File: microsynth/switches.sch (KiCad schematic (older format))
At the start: 37 parts, among them SW12 SOURCE, SW13 THUMBWEEL, SW14 SW_SPDT, SW15 SW_SPDT, SW16 SW_SPDT, SW17 SW_SPDT, SW2 RANGE, SW21 SW_Rotary2x6, SW3 SW_DPTT_SELECTOR, SW4 SW_DPTT_SELECTOR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

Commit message: Consolidate switches
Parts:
- SW12: value SOURCE -> SW_DP3T; footprint Buttons_Switches_ThroughHole:G-1128S-1110 -> microsynth:11-SS-23-832C; Value (none) -> THUMBWHEEL SOURCE
- SW13: value THUMBWEEL -> SW_DP3T; footprint Buttons_Switches_ThroughHole:G-1128S-1110 -> microsynth:11-SS-23-832C; Value (none) -> THUMBWHEEL DEST
- SW14, SW15, SW16, SW17, SW5: footprint Buttons_Switches_ThroughHole:GF-624-6014 -> microsynth:11-SS-22-701C
- SW2: value RANGE -> SW_Rotary2x6; Label Range -> VCO RANGE
- SW21: footprint Button_Switch_THT:SR2612F-0304-18R0B-D8-N -> microsynth:SR2612F-0304-18R0B-D8-N; Label (none) -> VCO2_SHAPE
- SW3, SW4, SW6: value SW_DPTT_SELECTOR -> SW_DP3T; footprint Buttons_Switches_ThroughHole:G-1128S-1110 -> microsynth:11-SS-23-832C
- SW3: value SW_DPTT_SELECTOR -> SW_DP3T; footprint Buttons_Switches_ThroughHole:G-1128S-1110 -> microsynth:11-SS-23-832C; Value (none) -> VCO1 SHAPE
- SW4: value SW_DPTT_SELECTOR -> SW_DP3T; footprint Buttons_Switches_ThroughHole:G-1128S-1110 -> microsynth:11-SS-23-832C; Label (none) -> SUBOCTAVES
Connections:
- wire segments 203 -> 199
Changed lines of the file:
@@
 AR Path="/5E475532/5E4ABA98" Ref="SW6"  Part="2"
 F 0 "SW6" H 6294 3079 50  0000 L CNN
-F 1 "SW_DPTT_SELECTOR" H 6294 2988 50  0000 L CNN
-F 2 "Buttons_Switches_ThroughHole:G-1128S-1110" H 6100 2950 50  0001 C CNN
+F 1 "SW_DP3T" H 6294 2988 50  0000 L CNN
+F 2 "microsynth:11-SS-23-832C" H 6100 2950 50  0001 C CNN
 F 3 "" H 6100 2950 50  0001 C CNN
 	2    6100 2950
@@
 AR Path="/5E475532/5E4BC6EF" Ref="SW3"  Part="1"
 F 0 "SW3" H 7594 1338 50  0000 L CNN
-F 1 "SW_DPTT_SELECTOR" H 7594 1247 50  0000 L CNN
-F 2 "Buttons_Switches_ThroughHole:G-1128S-1110" H 7400 1350 50  0001 C CNN
+F 1 "SW_DP3T" H 7594 1247 50  0000 L CNN
+F 2 "microsynth:11-SS-23-832C" H 7400 1350 50  0001 C CNN
 F 3 "" H 7400 1350 50  0001 C CNN
 	1    7400 1350
@@
 AR Path="/5E475532/5E4BCFE7" Ref="SW3"  Part="2"
 F 0 "SW3" H 7594 1379 50  0000 L CNN
-F 1 "SW_DPTT_SELECTOR" H 7594 1288 50  0000 L CNN
-F 2 "Buttons_Switches_ThroughHole:G-1128S-1110" H 7400 1250 50  0001 C CNN
+F 1 "SW_DP3T" H 7594 1288 50  0000 L CNN
+F 2 "microsynth:11-SS-23-832C" H 7400 1250 50  0001 C CNN
 F 3 "" H 7400 1250 50  0001 C CNN
+F 4 "VCO1 SHAPE" H 8050 1400 50  0000 C CNN "Value"
 	2    7400 1250
 	1    0    0    -1
@@
 AR Path="/5E475532/5E4C21F7" Ref="SW4"  Part="1"
 F 0 "SW4" H 9344 1338 50  0000 L CNN
-F 1 "SW_DPTT_SELECTOR" H 9344 1247 50  0000 L CNN
-F 2 "Buttons_Switches_ThroughHole:G-1128S-1110" H 9150 1350 50  0001 C CNN
+F 1 "SW_DP3T" H 9344 1247 50  0000 L CNN
+F 2 "microsynth:11-SS-23-832C" H 9150 1350 50  0001 C CNN
 F 3 "" H 9150 1350 50  0001 C CNN
 	1    9150 1350
-	1    0    0    -1
-$EndComp
-$Comp
-L microsynth-rescue:SW_DPTT_SELECTOR-Switch SW4
-U 2 1 5E4C2687
-P 9150 1250
-AR Path="/5E4C2687" Ref="SW4"  Part="2"
-AR Path="/5E475532/5E4C2687" Ref="SW4"  Part="2"
-F 0 "SW4" H 9344 1379 50  0000 L CNN
-F 1 "SW_DPTT_SELECTOR" H 9344 1288 50  0000 L CNN
-F 2 "Buttons_Switches_ThroughHole:G-1128S-1110" H 9150 1250 50  0001 C CNN
-F 3 "" H 9150 1250 50  0001 C CNN
-	2    9150 1250
 	1    0    0    -1
 $EndComp
@@
 NoConn ~ 9100 1550
 Wire Wire Line
-	9100 1050 9100 1300
-Wire Wire Line
-	9100 1300 9200 1300
-Wire Wire Line
-	9200 1300 9200 1550
-Wire Wire Line
-	9300 1550 9300 1250
-Wire Wire Line
-	9300 1250 9200 1250
-Wire Wire Line
-	9200 1250 9200 1050
-Wire Wire Line
 	7450 1550 7450 1750
 Wire Wire Line
@@
 Connection ~ 8550 1750
 Wire Wire Line
-	9300 1750 9300 1550
-Wire Wire Line
 	8550 1750 9300 1750
-Connection ~ 9300 1550
 $Comp
 L Device:R R80
@@
 Wire Wire Line
 	9200 1900 9200 1550
-Connection ~ 9200 1550
 Wire Wire Line
 	9300 1050 9300 950
@@
 U 1 1 5E4E1AE1
 P 9650 3100
-F 0 "U22" H 9650 3581 50  0000 C CNN
-F 1 "4013" H 9650 3490 50  0000 C CNN
+F 0 "U22" H 9700 3100 50  0000 C CNN
+F 1 "4013" H 9800 3350 50  0000 C CNN
 F 2 "Package_DIP:DIP-14_W7.62mm_LongPads" H 9650 3100 50  0001 C CNN
 F 3 "http://www.onsemi.com/pub/Collateral/MC14013B-D.PDF" H 9650 3100 50  0001 C CNN
@@
 F 0 "SW5" V 10604 1112 50  0000 R CNN
 F 1 "SW_SPDT" V 10695 1112 50  0000 R CNN
-F 2 "Buttons_Switches_ThroughHole:GF-624-6014" H 10650 1300 50  0001 C CNN
+F 2 "microsynth:11-SS-22-701C" H 10650 1300 50  0001 C CNN
 F 3 "~" H 10650 1300 50  0001 C CNN
 	1    10650 1300
@@
 U 2 1 5E4E234D
 P 9650 4350
-F 0 "U22" H 9650 4831 50  0000 C CNN
-F 1 "4013" H 9650 4740 50  0000 C CNN
+F 0 "U22" H 9700 4350 50  0000 C CNN
+F 1 "4013" H 9500 4600 50  0000 C CNN
 F 2 "Package_DIP:DIP-14_W7.62mm_LongPads" H 9650 4350 50  0001 C CNN
 F 3 "http://www.onsemi.com/pub/Collateral/MC14013B-D.PDF" H 9650 4350 50  0001 C CNN
@@
 P 1700 6350
 F 0 "SW2" H 1750 7221 50  0000 C CNN
-F 1 "RANGE" H 1750 7130 50  0000 C CNN
+F 1 "SW_Rotary2x6" H 1750 7130 50  0000 C CNN
 F 2 "MyKi_TH_Panel_Controls:SW_Rotary4+12" H 1600 6950 50  0001 C CNN
 F 3 "https://www.tme.eu/Document/ecc8d6706892f543e4658b0fb9f5b772/sr261112.pdf" H 1600 6950 50  0001 C CNN
-F 4 "Range" H 1750 7039 50  0000 C CNN "Label"
+F 4 "VCO RANGE" H 1750 7039 50  0000 C CNN "Label"
 F 5 "SR26NS1-2-6-M10-38R6" H 1700 6350 50  0001 C CNN "Product#"
 	1    1700 6350
@@
 AR Path="/5E475532/5E4A877E" Ref="SW6"  Part="1"
 F 0 "SW6" H 2894 2738 50  0000 L CNN
-F 1 "SW_DPTT_SELECTOR" H 2894 2647 50  0000 L CNN
-F 2 "Buttons_Switches_ThroughHole:G-1128S-1110" H 2700 2750 50  0001 C CNN
+F 1 "SW_DP3T" H 2894 2647 50  0000 L CNN
+F 2 "microsynth:11-SS-23-832C" H 2700 2750 50  0001 C CNN
 F 3 "" H 2700 2750 50  0001 C CNN
 	1    2700 2750
@@
 F 0 "SW17" H 3600 2635 50  0000 C CNN
 F 1 "SW_SPDT" H 3600 2544 50  0000 C CNN
-F 2 "Buttons_Switches_ThroughHole:GF-624-6014" H 3600 2350 50  0001 C CNN
+F 2 "microsynth:11-SS-22-701C" H 3600 2350 50  0001 C CNN
 F 3 "~" H 3600 2350 50  0001 C CNN
 	1    3600 2350
@@
 F 0 "SW16" H 3600 2135 50  0000 C CNN
 F 1 "SW_SPDT" H 3600 2044 50  0000 C CNN
-F 2 "Buttons_Switches_ThroughHole:GF-624-6014" H 3600 1850 50  0001 C CNN
+F 2 "microsynth:11-SS-22-701C" H 3600 1850 50  0001 C CNN
 F 3 "~" H 3600 1850 50  0001 C CNN
 	1    3600 1850
@@
 F 0 "SW15" H 3600 1635 50  0000 C CNN
 F 1 "SW_SPDT" H 3600 1544 50  0000 C CNN
-F 2 "Buttons_Switches_ThroughHole:GF-624-6014" H 3600 1350 50  0001 C CNN
+F 2 "microsynth:11-SS-22-701C" H 3600 1350 50  0001 C CNN
 F 3 "~" H 3600 1350 50  0001 C CNN
 	1    3600 1350
@@
 F 0 "SW14" H 3600 1135 50  0000 C CNN
 F 1 "SW_SPDT" H 3600 1044 50  0000 C CNN
-F 2 "Buttons_Switches_ThroughHole:GF-624-6014" H 3600 850 50  0001 C CNN
+F 2 "microsynth:11-SS-22-701C" H 3600 850 50  0001 C CNN
 F 3 "~" H 3600 850 50  0001 C CNN
 	1    3600 850
@@
 AR Path="/5E475532/5EC4EDF0" Ref="SW12"  Part="1"
 F 0 "SW12" H 5594 4488 50  0000 L CNN
-F 1 "SOURCE" H 5594 4397 50  0000 L CNN
-F 2 "Buttons_Switches_ThroughHole:G-1128S-1110" H 5400 4500 50  0001 C CNN
+F 1 "SW_DP3T" H 5594 4397 50  0000 L CNN
+F 2 "microsynth:11-SS-23-832C" H 5400 4500 50  0001 C CNN
 F 3 "" H 5400 4500 50  0001 C CNN
+F 4 "THUMBWHEEL SOURCE" H 5600 4900 50  0000 C CNN "Value"
 	1    5400 4500
 	1    0    0    -1
@@
 AR Path="/5E475532/5EC508E1" Ref="SW12"  Part="2"
 F 0 "SW12" H 5594 4629 50  0000 L CNN
-F 1 "SOURCE" H 5594 4538 50  0000 L CNN
-F 2 "Buttons_Switches_ThroughHole:G-1128S-1110" H 5400 4500 50  0001 C CNN
+F 1 "SW_DP3T" H 5594 4538 50  0000 L CNN
+F 2 "microsynth:11-SS-23-832C" H 5400 4500 50  0001 C CNN
 F 3 "" H 5400 4500 50  0001 C CNN
+F 4 "THUMBWHEEL SOURCE" H 5600 4900 50  0000 C CNN "Value"
 	2    5400 4500
 	1    0    0    -1
@@
 AR Path="/5E475532/5EC8F4DB" Ref="SW13"  Part="1"
 F 0 "SW13" H 7394 4438 50  0000 L CNN
-F 1 "THUMBWEEL" H 7394 4347 50  0000 L CNN
-F 2 "Buttons_Switches_ThroughHole:G-1128S-1110" H 7200 4450 50  0001 C CNN
+F 1 "SW_DP3T" H 7394 4347 50  0000 L CNN
+F 2 "microsynth:11-SS-23-832C" H 7200 4450 50  0001 C CNN
 F 3 "" H 7200 4450 50  0001 C CNN
+F 4 "THUMBWHEEL DEST" H 7200 4850 50  0000 C CNN "Value"
 	1    7200 4450
 	1    0    0    -1
@@
 AR Path="/5E475532/5EC90227" Ref="SW13"  Part="2"
 F 0 "SW13" H 7394 4579 50  0000 L CNN
-F 1 "THUMBWEEL" H 7394 4488 50  0000 L CNN
-F 2 "Buttons_Switches_ThroughHole:G-1128S-1110" H 7200 4450 50  0001 C CNN
+F 1 "SW_DP3T" H 7394 4488 50  0000 L CNN
+F 2 "microsynth:11-SS-23-832C" H 7200 4450 50  0001 C CNN
 F 3 "" H 7200 4450 50  0001 C CNN
+F 4 "THUMBWHEEL DEST" H 7200 4850 50  0000 C CNN "Value"
 	2    7200 4450
 	1    0    0    -1
@@
 F 0 "SW21" H 1850 2831 50  0000 C CNN
 F 1 "SW_Rotary2x6" H 1850 2740 50  0000 C CNN
-F 2 "Button_Switch_THT:SR2612F-0304-18R0B-D8-N" H 1700 2650 50  0001 C CNN
+F 2 "microsynth:SR2612F-0304-18R0B-D8-N" H 1700 2650 50  0001 C CNN
 F 3 "https://www.taydaelectronics.com/datasheets/A-1891.pdf" H 1700 2650 50  0001 C CNN
+F 4 "VCO2_SHAPE" H 1400 2850 50  0000 C CNN "Label"
 	1    1800 2050
 	-1   0    0    -1
@@
 NoConn ~ 1300 2550
 NoConn ~ 1300 2650
+Wire Wire Line
+	9300 1750 9300 1550
+$Comp
+L microsynth-rescue:SW_DPTT_SELECTOR-Switch SW4
+U 2 1 5E4C2687
+P 9150 1250
+AR Path="/5E4C2687" Ref="SW4"  Part="2"
+AR Path="/5E475532/5E4C2687" Ref="SW4"  Part="2"
+F 0 "SW4" H 9344 1379 50  0000 L CNN
+F 1 "SW_DP3T" H 9344 1288 50  0000 L CNN
+F 2 "microsynth:11-SS-23-832C" H 9150 1250 50  0001 C CNN
+F 3 "" H 9150 1250 50  0001 C CNN
+F 4 "SUBOCTAVES" H 9250 1600 50  0000 C CNN "Label"
+	2    9150 1250
+	1    0    0    -1
+$EndComp
+Wire Wire Line
+	9300 1550 9200 1050
+Connection ~ 9300 1550
+Wire Wire Line
+	9200 1550 9100 1050
+Connection ~ 9200 1550
 $EndSCHEMATC

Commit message: Consolidate all(?) switches
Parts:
- RV20, RV28: footprint 4ms_Potentiometer:Pot_16mm_NoDet_RV16AF-4A -> microsynth:Pot_16mm_NoDet_RV16AF-4A
- SW12, SW13, SW3, SW4, SW6: symbol microsynth-rescue:SW_DPTT_SELECTOR-Switch -> pe_microsynth:SW_DPTT_SELECTOR-Switch
- SW2: footprint MyKi_TH_Panel_Controls:SW_Rotary4+12 -> microsynth:SW_Rotary4+12
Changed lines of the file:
@@
 $EndDescr
 $Comp
-L microsynth-rescue:SW_DPTT_SELECTOR-Switch SW6
+L pe_microsynth:SW_DPTT_SELECTOR-Switch SW6
 U 2 1 5E4ABA98
 P 6100 2950
@@
 $EndComp
 $Comp
-L microsynth-rescue:SW_DPTT_SELECTOR-Switch SW3
+L pe_microsynth:SW_DPTT_SELECTOR-Switch SW3
 U 1 1 5E4BC6EF
 P 7400 1350
@@
 $EndComp
 $Comp
-L microsynth-rescue:SW_DPTT_SELECTOR-Switch SW3
+L pe_microsynth:SW_DPTT_SELECTOR-Switch SW3
 U 2 1 5E4BCFE7
 P 7400 1250
@@
 NoConn ~ 7250 1550
 $Comp
-L microsynth-rescue:SW_DPTT_SELECTOR-Switch SW4
+L pe_microsynth:SW_DPTT_SELECTOR-Switch SW4
 U 1 1 5E4C21F7
 P 9150 1350
@@
 F 0 "SW2" H 1750 7221 50  0000 C CNN
 F 1 "SW_Rotary2x6" H 1750 7130 50  0000 C CNN
-F 2 "MyKi_TH_Panel_Controls:SW_Rotary4+12" H 1600 6950 50  0001 C CNN
+F 2 "microsynth:SW_Rotary4+12" H 1600 6950 50  0001 C CNN
 F 3 "https://www.tme.eu/Document/ecc8d6706892f543e4658b0fb9f5b772/sr261112.pdf" H 1600 6950 50  0001 C CNN
 F 4 "VCO RANGE" H 1750 7039 50  0000 C CNN "Label"
@@
 	2200 2050 2400 2050
 $Comp
-L microsynth-rescue:SW_DPTT_SELECTOR-Switch SW6
+L pe_microsynth:SW_DPTT_SELECTOR-Switch SW6
 U 1 1 5E4A877E
 P 2700 2750
@@
 F 0 "RV20" H 2480 1746 50  0000 R CNN
 F 1 "10kLOG" H 2480 1655 50  0000 R CNN
-F 2 "4ms_Potentiometer:Pot_16mm_NoDet_RV16AF-4A" H 2550 1700 50  0001 C CNN
+F 2 "microsynth:Pot_16mm_NoDet_RV16AF-4A" H 2550 1700 50  0001 C CNN
 F 3 "~" H 2550 1700 50  0001 C CNN
 F 4 "VCO2 Level" H 2450 1800 50  0000 R BNN "Label"
@@
 F 0 "RV28" H 3980 4646 50  0000 R CNN
 F 1 "1kLIN" H 3980 4555 50  0000 R CNN
-F 2 "4ms_Potentiometer:Pot_16mm_NoDet_RV16AF-4A" H 4050 4600 50  0001 C CNN
+F 2 "microsynth:Pot_16mm_NoDet_RV16AF-4A" H 4050 4600 50  0001 C CNN
 F 3 "~" H 4050 4600 50  0001 C CNN
 F 4 "Sweep" H 3950 4450 50  0000 R BNN "Label"
@@
 	6400 5000 6400 4900
 $Comp
-L microsynth-rescue:SW_DPTT_SELECTOR-Switch SW12
+L pe_microsynth:SW_DPTT_SELECTOR-Switch SW12
 U 1 1 5EC4EDF0
 P 5400 4500
@@
 $EndComp
 $Comp
-L microsynth-rescue:SW_DPTT_SELECTOR-Switch SW12
+L pe_microsynth:SW_DPTT_SELECTOR-Switch SW12
 U 2 1 5EC508E1
 P 5400 4500
@@
 	5550 3900 4950 3900
 $Comp
-L microsynth-rescue:SW_DPTT_SELECTOR-Switch SW13
+L pe_microsynth:SW_DPTT_SELECTOR-Switch SW13
 U 1 1 5EC8F4DB
 P 7200 4450
@@
 $EndComp
 $Comp
-L microsynth-rescue:SW_DPTT_SELECTOR-Switch SW13
+L pe_microsynth:SW_DPTT_SELECTOR-Switch SW13
 U 2 1 5EC90227
 P 7200 4450
@@
 	9300 1750 9300 1550
 $Comp
-L microsynth-rescue:SW_DPTT_SELECTOR-Switch SW4
+L pe_microsynth:SW_DPTT_SELECTOR-Switch SW4
 U 2 1 5E4C2687
 P 9150 1250

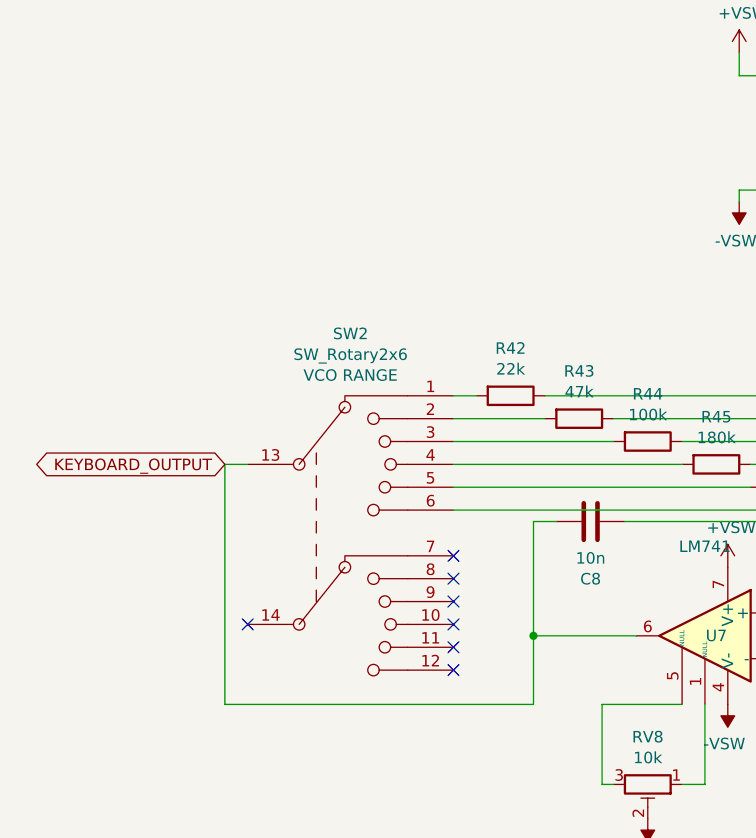
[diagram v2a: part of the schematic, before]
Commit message: Update tayda rotary switch footprints and layout
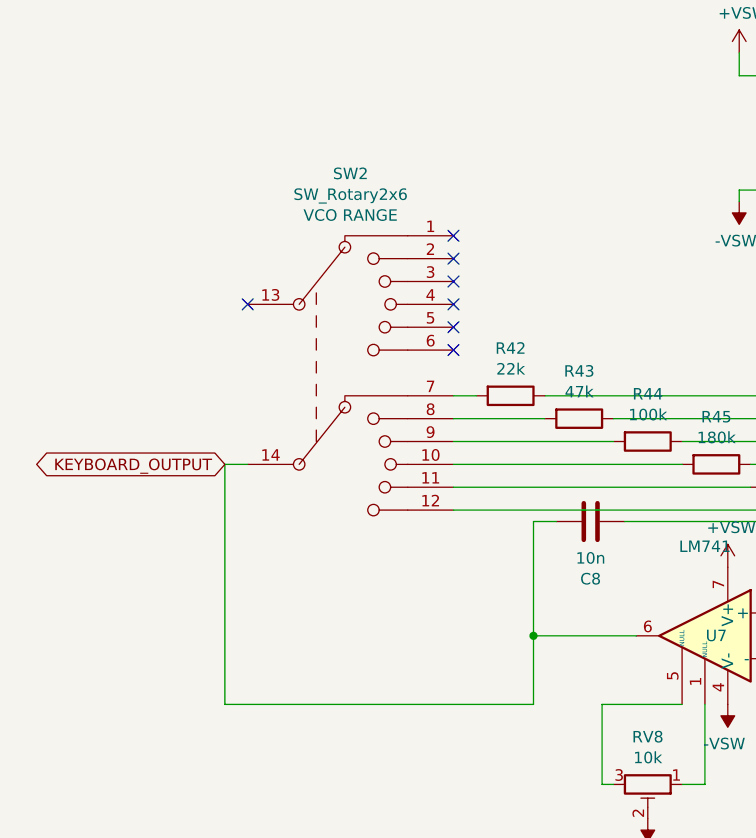
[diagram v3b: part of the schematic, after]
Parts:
- SW2: footprint microsynth:SW_Rotary4+12 -> microsynth:SR2511F-0206-(L)K0A-C9-S-3
- SW21: footprint microsynth:SR2612F-0304-18R0B-D8-N -> microsynth:SR2511F-0204-(L)K0A-C9-S-3
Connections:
- net KEYBOARD_IC7_PIN_6: now also SW2.14; no longer SW2.13
- net at SW2.1: no longer R42.2
- net at SW2.10: now also R45.2
- net at SW2.11: now also R46.1
- net at SW2.12: now also R46-1.1
- net at SW2.2: no longer R43.2
- net at SW2.3: no longer R44.2
- net at SW2.4: no longer R45.2
- net at SW2.5: no longer R46.1
- net at SW2.6: no longer R46-1.1
- net at SW2.7: now also R42.2
- net at SW2.8: now also R43.2
- net at SW2.9: now also R44.2
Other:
- moved on the sheet: SW2
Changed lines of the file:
@@
 Wire Wire Line
 	9350 3100 8800 3100
-NoConn ~ 2200 6850
-NoConn ~ 2200 6750
-NoConn ~ 2200 6650
-NoConn ~ 2200 6550
-NoConn ~ 2200 6450
-NoConn ~ 1300 6750
+NoConn ~ 2200 5450
+NoConn ~ 2200 5350
+NoConn ~ 2200 5250
+NoConn ~ 2200 5150
+NoConn ~ 2200 5050
+NoConn ~ 1300 5350
 $Comp
 L Switch:SW_Rotary2x6 SW2
 U 1 1 5E4793CB
-P 1700 6350
-F 0 "SW2" H 1750 7221 50  0000 C CNN
-F 1 "SW_Rotary2x6" H 1750 7130 50  0000 C CNN
-F 2 "microsynth:SW_Rotary4+12" H 1600 6950 50  0001 C CNN
-F 3 "https://www.tme.eu/Document/ecc8d6706892f543e4658b0fb9f5b772/sr261112.pdf" H 1600 6950 50  0001 C CNN
-F 4 "VCO RANGE" H 1750 7039 50  0000 C CNN "Label"
-F 5 "SR26NS1-2-6-M10-38R6" H 1700 6350 50  0001 C CNN "Product#"
-	1    1700 6350
+P 1700 5650
+F 0 "SW2" H 1750 6521 50  0000 C CNN
+F 1 "SW_Rotary2x6" H 1750 6430 50  0000 C CNN
+F 2 "microsynth:SR2511F-0206-(L)K0A-C9-S-3" H 1600 6250 50  0001 C CNN
+F 3 "https://www.tme.eu/Document/ecc8d6706892f543e4658b0fb9f5b772/sr261112.pdf" H 1600 6250 50  0001 C CNN
+F 4 "VCO RANGE" H 1750 6339 50  0000 C CNN "Label"
+F 5 "SR26NS1-2-6-M10-38R6" H 1700 5650 50  0001 C CNN "Product#"
+	1    1700 5650
 	1    0    0    -1
 $EndComp
@@
 NoConn ~ 2750 2950
 NoConn ~ 2850 2950
-NoConn ~ 2200 6950
+NoConn ~ 2200 5550
 Wire Wire Line
 	3200 5950 4500 5950
@@
 F 0 "SW21" H 1850 2831 50  0000 C CNN
 F 1 "SW_Rotary2x6" H 1850 2740 50  0000 C CNN
-F 2 "microsynth:SR2612F-0304-18R0B-D8-N" H 1700 2650 50  0001 C CNN
+F 2 "microsynth:SR2511F-0204-(L)K0A-C9-S-3" H 1700 2650 50  0001 C CNN
 F 3 "https://www.taydaelectronics.com/datasheets/A-1891.pdf" H 1700 2650 50  0001 C CNN
 F 4 "VCO2_SHAPE" H 1400 2850 50  0000 C CNN "Label"

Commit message: Add test points
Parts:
- added TP4: VCO2, TestPoint:TestPoint_Pad_D2.0mm, symbol Connector:TestPoint
- added TP5: VCO1, TestPoint:TestPoint_Pad_D2.0mm, symbol Connector:TestPoint
- SW21: symbol Switch:SW_Rotary3x4 -> pe_microsynth:SW_Rotary2x4
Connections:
- net LFO_TO_VR20_SLIDER: now also TP4.1
- net TO_VCF_IC20_3: now also TP5.1
- no-connect marks 28 -> 23
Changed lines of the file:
@@
 	7450 1550 7450 1750
 Wire Wire Line
-	7450 1750 8550 1750
+	7450 1750 7950 1750
 Wire Wire Line
 	6950 800  7350 800
@@
 Connection ~ 3250 1700
 Wire Wire Line
-	2700 1700 3250 1700
+	2700 1700 2800 1700
 Connection ~ 3250 1850
 Wire Wire Line
@@
 	3800 6250 2200 6250
 $Comp
-L Switch:SW_Rotary3x4 SW21
+L pe_microsynth:SW_Rotary2x4 SW21
 U 1 1 5E476048
-P 1800 2050
-F 0 "SW21" H 1850 2831 50  0000 C CNN
-F 1 "SW_Rotary2x6" H 1850 2740 50  0000 C CNN
-F 2 "microsynth:SR2511F-0204-(L)K0A-C9-S-3" H 1700 2650 50  0001 C CNN
-F 3 "https://www.taydaelectronics.com/datasheets/A-1891.pdf" H 1700 2650 50  0001 C CNN
-F 4 "VCO2_SHAPE" H 1400 2850 50  0000 C CNN "Label"
-	1    1800 2050
+P 1800 1700
+F 0 "SW21" H 1850 2481 50  0000 C CNN
+F 1 "SW_Rotary2x6" H 1850 2390 50  0000 C CNN
+F 2 "microsynth:SR2511F-0204-(L)K0A-C9-S-3" H 1700 2300 50  0001 C CNN
+F 3 "https://www.taydaelectronics.com/datasheets/A-1891.pdf" H 1700 2300 50  0001 C CNN
+F 4 "VCO2_SHAPE" H 1400 2500 50  0000 C CNN "Label"
+	1    1800 1700
 	-1   0    0    -1
 $EndComp
-NoConn ~ 2200 2550
-NoConn ~ 1300 2350
-NoConn ~ 1300 2450
-NoConn ~ 1300 2550
-NoConn ~ 1300 2650
 Wire Wire Line
 	9300 1750 9300 1550
@@
 	9200 1550 9100 1050
 Connection ~ 9200 1550
+$Comp
+L Connector:TestPoint TP5
+U 1 1 5EDEA929
+P 7950 1750
+F 0 "TP5" H 8050 1900 50  0000 L CNN
+F 1 "VCO1" H 8050 1800 50  0000 L CNN
+F 2 "TestPoint:TestPoint_Pad_D2.0mm" H 8150 1750 50  0001 C CNN
+F 3 "~" H 8150 1750 50  0001 C CNN
+	1    7950 1750
+	1    0    0    -1
+$EndComp
+Connection ~ 7950 1750
+Wire Wire Line
+	7950 1750 8550 1750
+$Comp
+L Connector:TestPoint TP4
+U 1 1 5EDEAFEB
+P 2800 1700
+F 0 "TP4" H 2900 1850 50  0000 L CNN
+F 1 "VCO2" H 2900 1750 50  0000 L CNN
+F 2 "TestPoint:TestPoint_Pad_D2.0mm" H 3000 1700 50  0001 C CNN
+F 3 "~" H 3000 1700 50  0001 C CNN
+	1    2800 1700
+	1    0    0    -1
+$EndComp
+Connection ~ 2800 1700
+Wire Wire Line
+	2800 1700 3250 1700
 $EndSCHEMATC
